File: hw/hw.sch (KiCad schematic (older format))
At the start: 44 parts, among them U1 74LS32, U10 74LS74, U2 Z80CPU, U3 74LS138, U4 74LS08, U5 CY7C199, U6 74LS299, U7 74HCT574, U8 74LS161, U9 74LS245, X1 CXO_DIP8

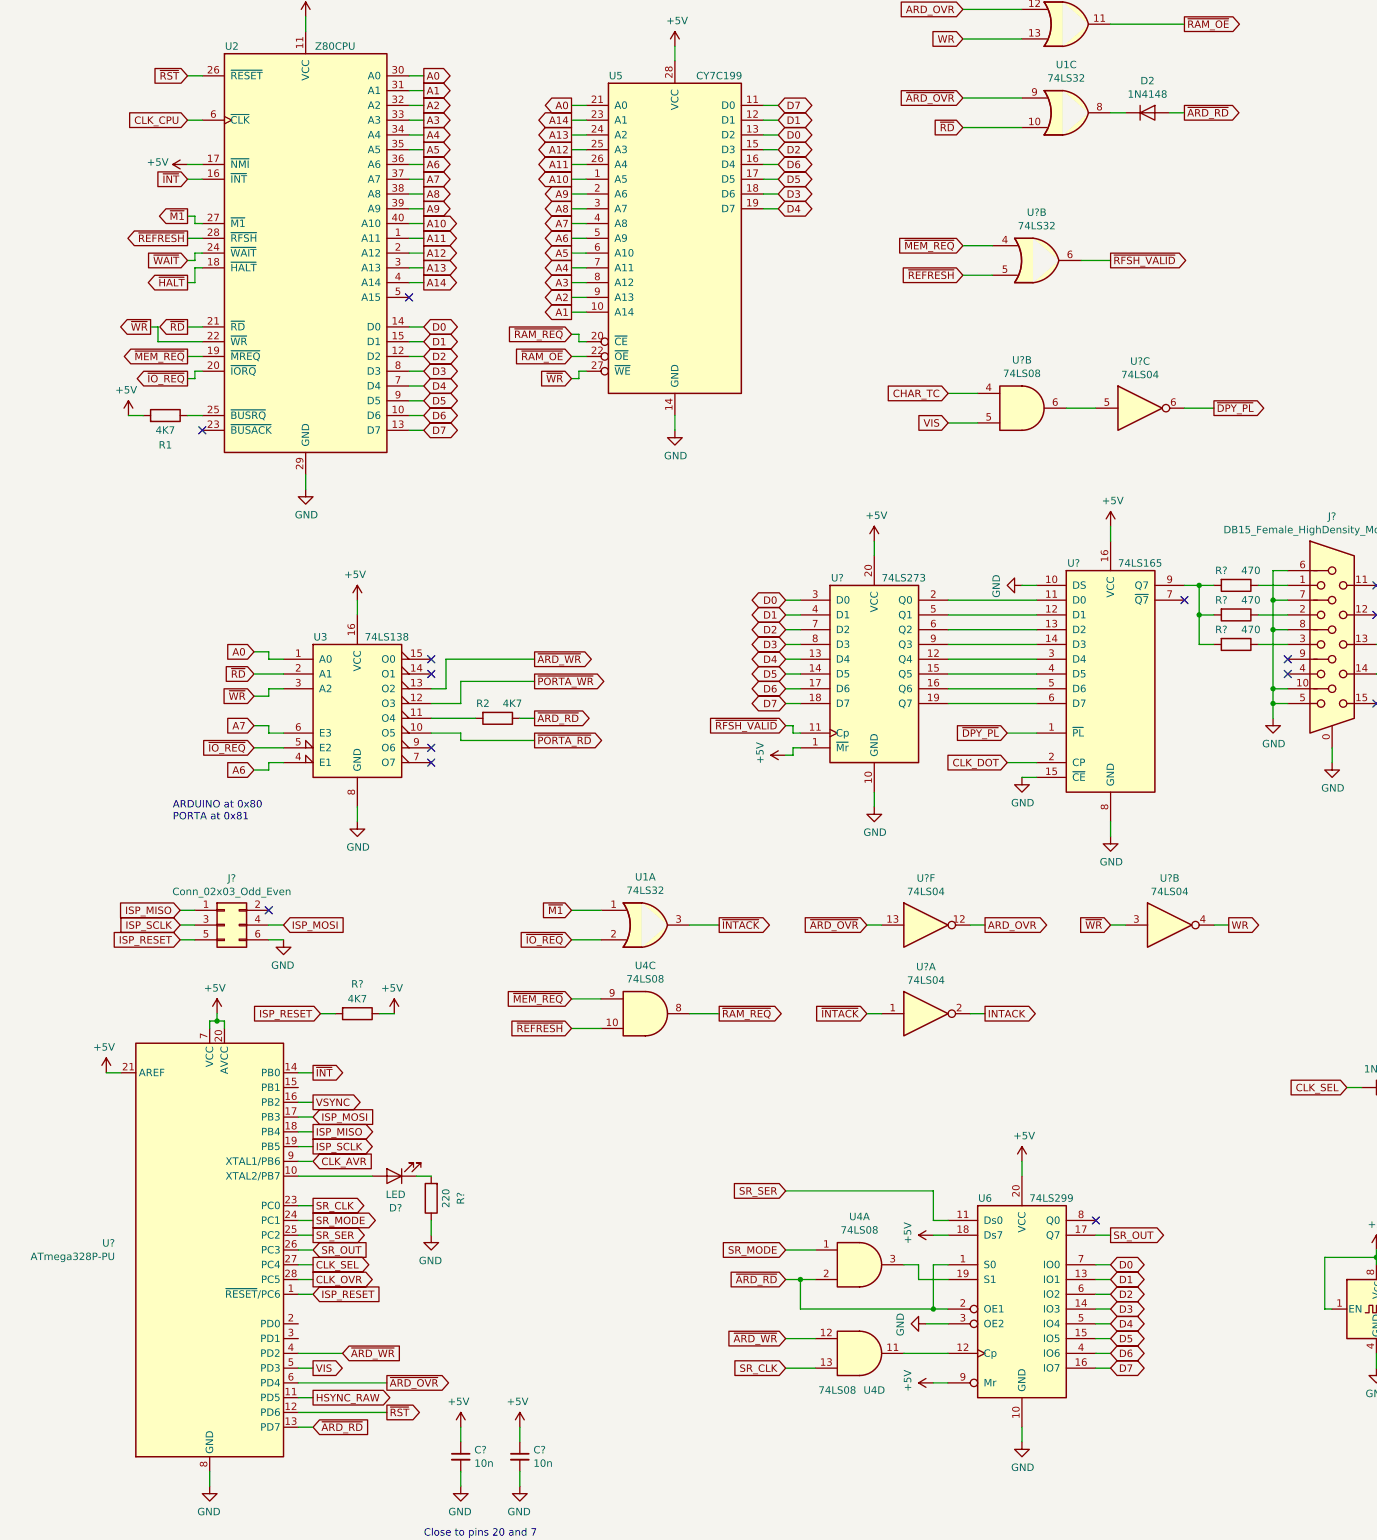
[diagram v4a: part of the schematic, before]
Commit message: start to tidy up AVR to/from CPU comms
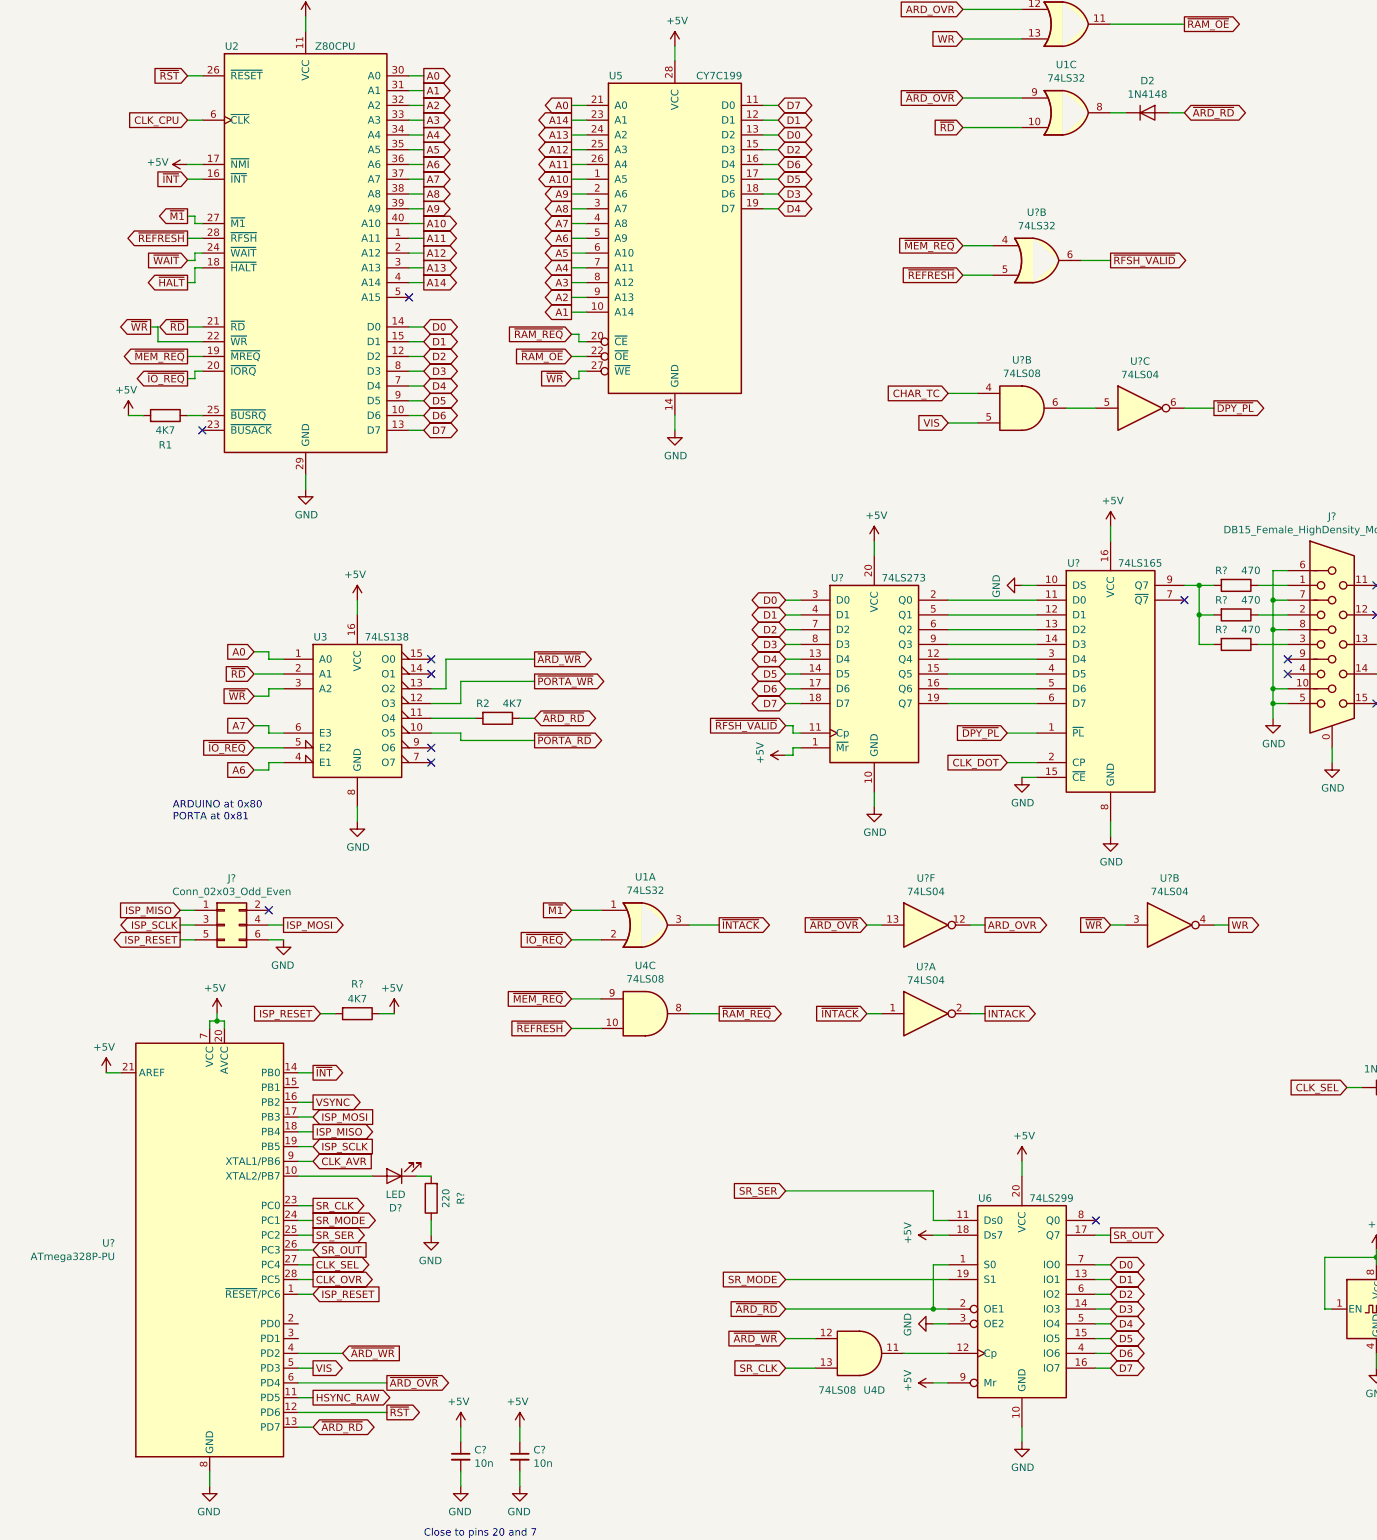
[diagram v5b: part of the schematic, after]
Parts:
- removed unit 1 of U4
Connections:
- net SR_MODE: now also U6.19 (S1)
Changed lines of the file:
@@
 	0    -1   -1   0
 $EndComp
-Text GLabel 5500 9200 0    50   Input ~ 0
-SR_MODE
-Text GLabel 5500 9400 0    50   Input ~ 0
-~ARD_RD
-Wire Wire Line
-	6450 9700 6600 9700
+Wire Wire Line
+	6500 9700 6600 9700
 Wire Wire Line
 	6300 9900 6600 9900
@@
 Wire Wire Line
 	2000 5400 2100 5400
-Text GLabel 3800 5600 2    50   Output ~ 0
+Text GLabel 3800 5600 2    50   BiDi ~ 0
 ~ARD_RD
 Text GLabel 11500 9000 2    50   Output ~ 0
@@
 	5700 10000 5500 10000
 Wire Wire Line
-	6300 9300 6400 9300
-Wire Wire Line
-	6400 9300 6400 9400
-Wire Wire Line
-	6400 9400 6600 9400
-Wire Wire Line
-	5500 9400 5600 9400
-Wire Wire Line
-	5700 9200 5500 9200
-Wire Wire Line
 	1450 2350 1550 2350
 Wire Wire Line
@@
 Wire Wire Line
 	1500 2450 1550 2450
-Wire Wire Line
-	5600 9400 5600 9600
-Connection ~ 5600 9400
-Wire Wire Line
-	5600 9400 5700 9400
 $Comp
 L power:GND #PWR011
 U 1 1 5D88A3F1
-P 6450 9700
-F 0 "#PWR011" H 6450 9450 50  0001 C CNN
-F 1 "GND" H 6455 9527 50  0000 C CNN
-F 2 "" H 6450 9700 50  0001 C CNN
-F 3 "" H 6450 9700 50  0001 C CNN
-	1    6450 9700
+P 6500 9700
+F 0 "#PWR011" H 6500 9450 50  0001 C CNN
+F 1 "GND" H 6505 9527 50  0000 C CNN
+F 2 "" H 6500 9700 50  0001 C CNN
+F 3 "" H 6500 9700 50  0001 C CNN
+	1    6500 9700
 	0    1    1    0
 $EndComp
@@
 	1    0    0    -1
 $EndComp
-Text GLabel 8200 1500 2    50   Output ~ 0
+Text GLabel 8200 1500 2    50   BiDi ~ 0
 ~ARD_RD
 Wire Wire Line
@@
 	1    3550 5600
 	0    1    1    0
-$EndComp
-$Comp
-L 74xx:74LS08 U4
-U 1 1 5E14BD34
-P 6000 9300
-F 0 "U4" H 6000 9625 50  0000 C CNN
-F 1 "74LS08" H 6000 9534 50  0000 C CNN
-F 2 "" H 6000 9300 50  0001 C CNN
-F 3 "http://www.ti.com/lit/gpn/sn74LS08" H 6000 9300 50  0001 C CNN
-	1    6000 9300
-	1    0    0    -1
 $EndComp
 $Comp
@@
 NoConn ~ 3100 5900
 Wire Wire Line
-	5600 9600 6500 9600
-Wire Wire Line
 	6700 1400 7100 1400
 $Comp
@@
 Wire Wire Line
 	6500 9100 6600 9100
-Wire Wire Line
-	6500 9300 6500 9600
-Connection ~ 6500 9600
-Wire Wire Line
-	6500 9600 6600 9600
 Text GLabel 1450 2650 0    50   Output ~ 0
 ~HALT
@@
 Wire Wire Line
 	2300 8400 2200 8400
-Text GLabel 2100 7000 2    50   Input ~ 0
+Text GLabel 2100 7000 2    50   Output ~ 0
 ISP_MOSI
 Wire Wire Line
@@
 Wire Wire Line
 	2300 8300 2200 8300
-Text GLabel 1400 7000 0    50   Input ~ 0
+Text GLabel 1400 7000 0    50   Output ~ 0
 ISP_SCLK
-Text GLabel 1400 7100 0    50   Input ~ 0
+Text GLabel 1400 7100 0    50   Output ~ 0
 ISP_RESET
 Text GLabel 2300 9500 2    50   Input ~ 0
@@
 Wire Wire Line
 	1500 7100 1400 7100
-Text GLabel 2300 8500 2    50   Output ~ 0
+Text GLabel 2300 8500 2    50   Input ~ 0
 ISP_SCLK
 Wire Wire Line
@@
 Wire Wire Line
 	2300 8000 2200 8000
-Text GLabel 2300 10400 2    50   Input ~ 0
+Text GLabel 2300 10400 2    50   BiDi ~ 0
 ~ARD_RD
 Wire Wire Line
@@
 Wire Wire Line
 	6700 1000 7100 1000
+Text GLabel 5500 9600 0    50   Input ~ 0
+~ARD_RD
+Wire Wire Line
+	5500 9600 6500 9600
+Text GLabel 5500 9400 0    50   Input ~ 0
+SR_MODE
+Wire Wire Line
+	5500 9400 6600 9400
+Wire Wire Line
+	6500 9300 6500 9600
+Connection ~ 6500 9600
+Wire Wire Line
+	6500 9600 6600 9600
 $EndSCHEMATC
